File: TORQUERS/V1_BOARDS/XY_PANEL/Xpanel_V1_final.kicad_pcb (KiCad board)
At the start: 4 copper layers, 82.6 x 98 mm, 98 parts, among them J1 F3311A7H121014E200, J2 F3311A7H121014E200, Q1 BSS138, Q10 MBT2222ADW1T1, Q11 BSS138, Q12 MBT2222ADW1T1, Q2 BSS138, Q3 BSS138, Q4 MBT2222ADW1T1, Q5 BSS138, Q6 MBT2222ADW1T1, Q7 BSS138, Q8 BSS138, Q9 BSS138, U1 LTC3130EUDC-1-PBF, U2 DRV8830DGQ, U3 OPT4001DTST, U4 LTC3130EUDC-1-PBF

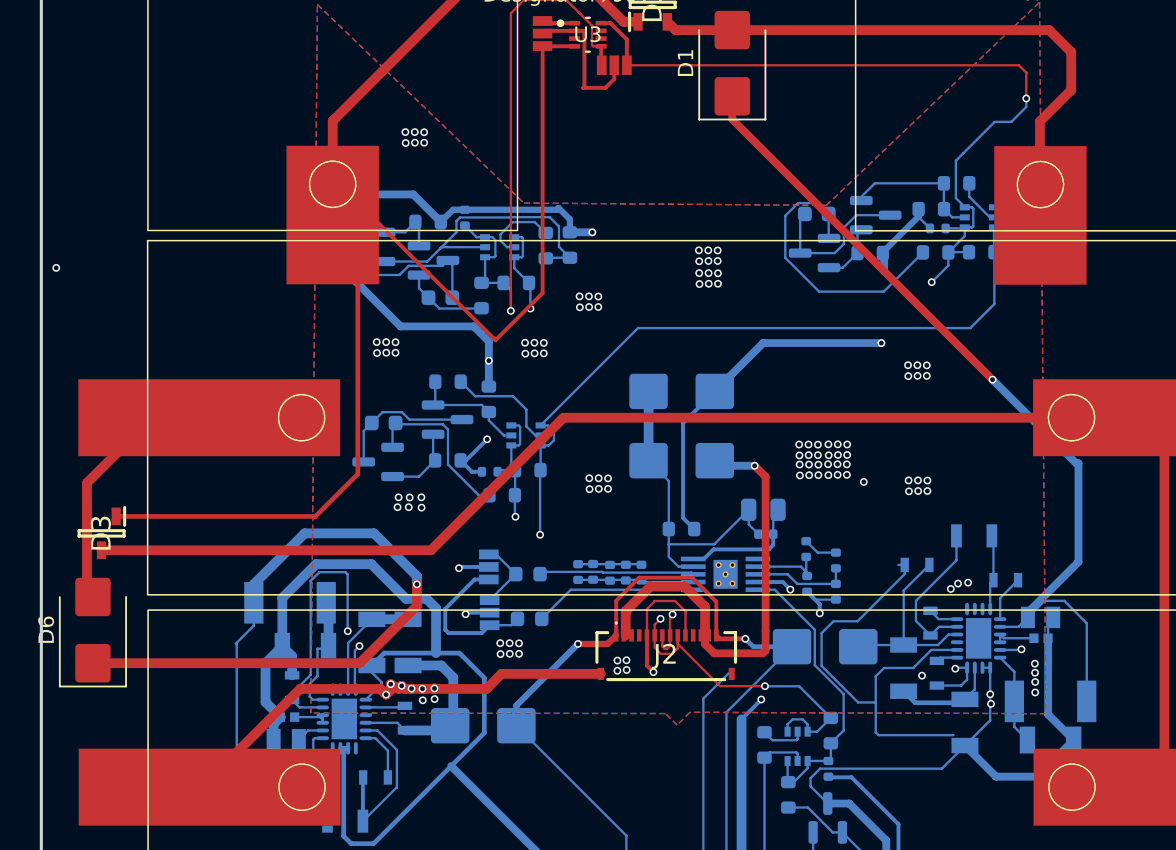
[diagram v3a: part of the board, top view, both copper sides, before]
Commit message: Cleared DRC and signoff
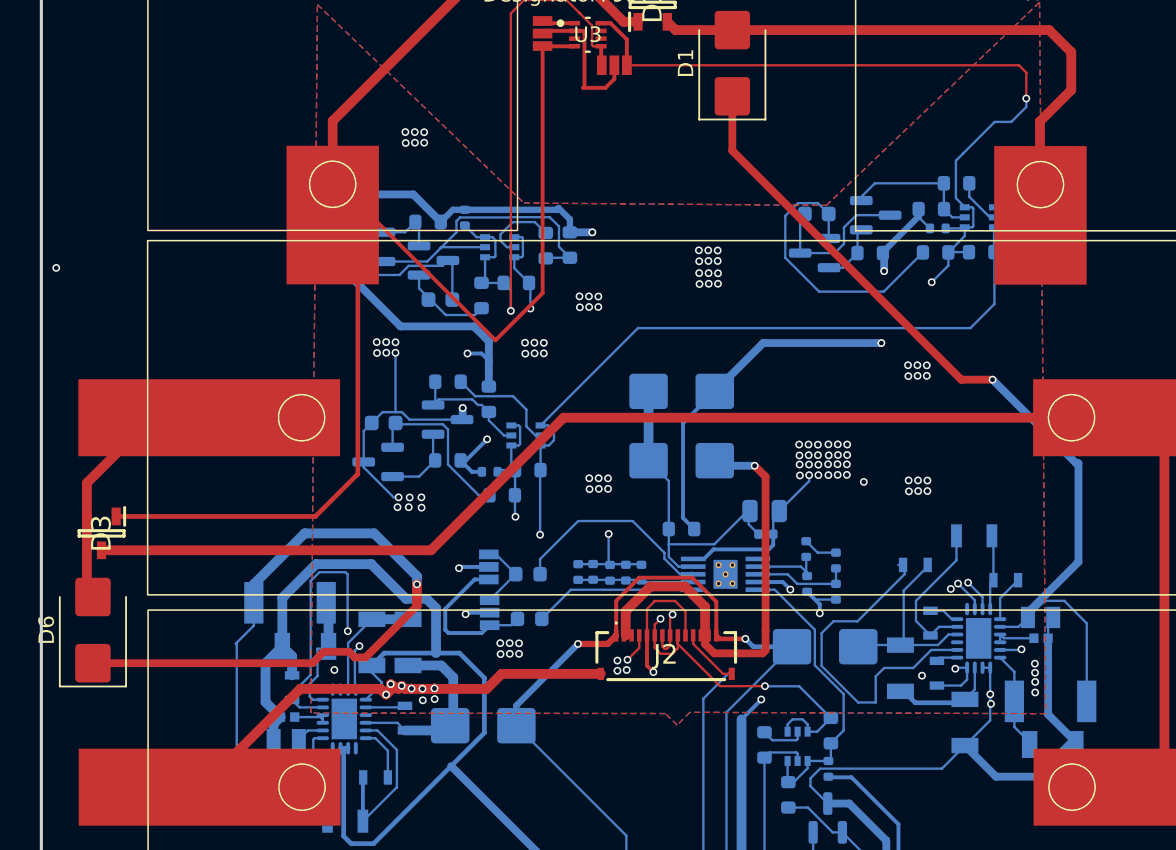
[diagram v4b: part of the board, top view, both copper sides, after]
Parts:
- moved R9 0.32 mm to (176.2, 116.4)
- moved R13 0.21 mm to (166.4, 111.4)
- moved C10 0.12 mm to (136.5, 87.5)
- moved C6 0.11 mm to (157.5, 101.2)
- moved C9 0.11 mm to (167.3, 104.7)
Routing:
- net GND: track 352.6 -> 375.8 mm, vias 113 -> 116
- net Net-(U1-EXTVCC): track 29.4 -> 22.3 mm
- net Net-(U2-OUT1): track 10.1 -> 14.0 mm
- net +3.3V: track 186.7 -> 189.3 mm
- net Net-(D1-K): track 56.6 -> 57.8 mm

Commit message: cleared All warnings and DRC
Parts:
- moved R33 0.06 mm to (168.8, 82.9)
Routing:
- net SDA_SUN: track 50.8 -> 48.4 mm, vias 2 -> 1
- net coils: track 34691.2 -> 34690.4 mm

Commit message: added logo
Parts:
- added .: ., argus:Argus LOGO, F.Cu at (148.4, 78.8)
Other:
- board text added: "XY SIDE PANEL BOARD ARGUS1 REV1.0"
